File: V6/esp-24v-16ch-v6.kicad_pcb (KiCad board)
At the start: 4 copper layers, 128 x 67.8 mm, 327 parts, among them J1 ENTRADAS 1-8, J2 GNDIO, J3 ENTRADAS 9-16, J4 SAÍDAS 1-8, J5 SAÍDAS 9-16, J6 VIN, J7 USB_C_Receptacle_USB2.0, J8 ETHERNET, J9 SENSORS, Q1 WPM2015-3/TR, Q10 MMBT2222A, Q11 MMBT2222A, Q12 MMBT2222A, Q13 MMBT2222A, Q14 MMBT2222A, Q15 MMBT2222A, Q16 MMBT2222A, Q17 MMBT2222A, Q18 MMBT2222A, Q19 MMBT2222A, Q2 MMUN2211LT3G, Q3 UMH3N, Q4 MMBT2222A, Q5 MMBT2222A, Q6 MMBT2222A, Q7 MMBT2222A, Q8 MMBT2222A, Q9 MMBT2222A, SW1 RESET, SW2 1WIRE_SEL, U1 SY8089A1AAC, U10 OR-3H7-4, U11 OR-3H7-4, U12 OR-3H7-4, U13 OR-3H7-4, U2 TX4138, U3 CH340K, U4 ESP32-WROOM-32UE-N16, U5 LAN8710A, U6 MCP23008-xSS, U7 MCP23008-xSS, U8 MCP23017x-x-SS, U9 DS2482S-100

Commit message: V6
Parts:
- removed Ref**: Val**, Tales:Grandmas_small_silk
- added G***: LOGO, Tales:eumesmo_teste1, F.Cu at (210.3, 103.8)

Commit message: Layout improvements
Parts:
- G***: footprint Tales:eumesmo_teste1 -> Tales:Eumesmo_small_silk
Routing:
- net /LAN/EMACRX: track 45.8 -> 51.8 mm
- net /LAN/EMACTXEN: track 35.6 -> 39.4 mm
- net /I2C Devices/I2CSCL: track 95.1 -> 97.1 mm
- net /LAN/EMACTXD0: track 40.4 -> 39.2 mm
- net /I2C Devices/MCPIN1INT: track 30.3 -> 29.3 mm
- net /LAN/EMACTXD1: track 40.5 -> 39.5 mm
- net +3V3: track 75.3 -> 74.6 mm

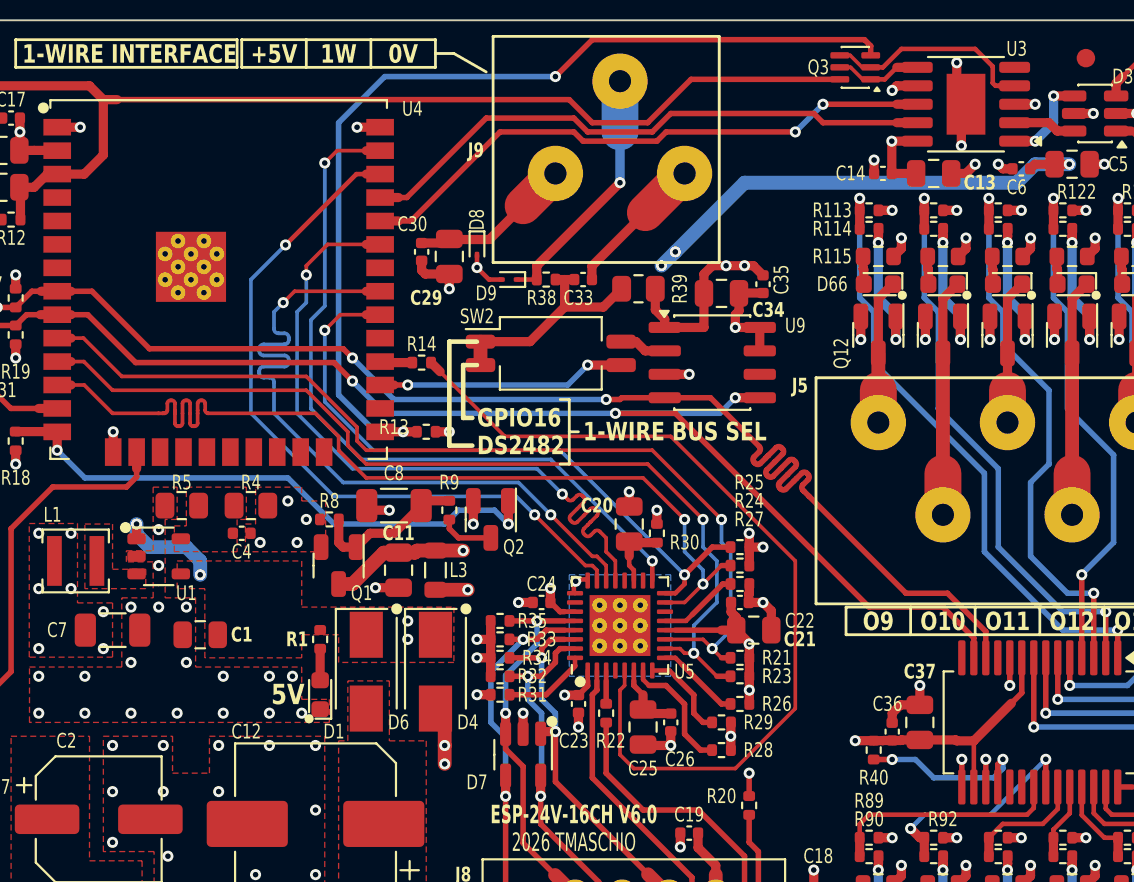
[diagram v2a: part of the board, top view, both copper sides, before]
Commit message: Update V6 PCB routing, fabrication and production files
Modify V6 board assets: updated esp-24v-16ch board image and kicad_pcb with numerous trace/via relocations, segment coordinate changes, updated UUIDs, and net/routing adjustments (LAN/EMAC, USB/5V, +3V3, +5V). Also updated fabrication-toolkit options, production ZIP, and netlist.ipc to reflect the revised layout. These changes appear to be routing cleanup and power/IO rework for the V6 revision.
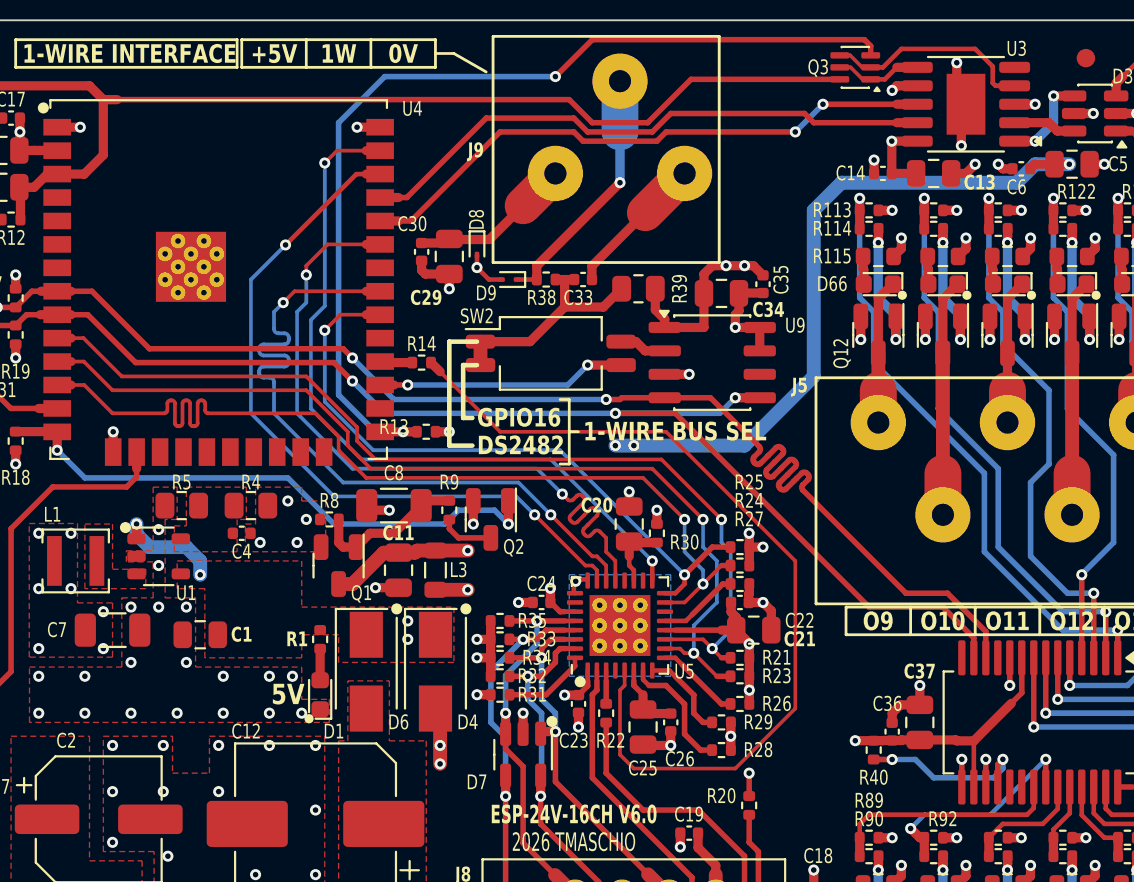
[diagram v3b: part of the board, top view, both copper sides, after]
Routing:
- net /Power/5VUSB: track 79.5 -> 82.8 mm
